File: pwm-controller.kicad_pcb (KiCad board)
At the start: 2 copper layers, 50 x 50 mm, 75 parts, among them J2 OUT-, J4 POWER, J5 OUT+, J6 DEBUG, J7 I2C, Q1 AO3400A, Q10 MMBT5551, Q11 MMBT5551, Q12 MMBT5401, Q2 AO3400A, Q3 AO3400A, Q4 AO3400A, Q5 AO3400A, Q6 AO3400A, Q7 MMBT5551, Q8 MMBT5551, Q9 MMBT5401, SW1 EC12D1524403, U1 L78L09_SOT89, U3 STM8S003F3Px, U4 HT7533-1-SOT89

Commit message: ready?
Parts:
- removed C13, C14, C15, C16, C17, C18, C19, C20: 100n/50, Capacitor_SMD:C_0402_1005Metric
- removed C9: 1u/50, Capacitor_SMD:C_0603_1608Metric
- removed Q11, Q8: MMBT5551, Package_TO_SOT_SMD:SOT-23
- removed Q3, Q6: AO3400A, Package_TO_SOT_SMD:SOT-23
- removed R18, R23, R25, R27: 4.7k, Resistor_SMD:R_0402_1005Metric
- removed R19, R28: 1k, Resistor_SMD:R_0402_1005Metric
- removed U4: HT7533-1-SOT89, Package_TO_SOT_SMD:SOT-89-3
- added TP1: TP5V, TestPoint:TestPoint_Pad_D2.0mm, F.Cu at (95.2, 87.3)
- C3, C4: value 100n/50 -> 3.3n
- Q1, Q2, Q4, Q5: value AO3400A -> NTMS4807; footprint Package_TO_SOT_SMD:SOT-23 -> mark:NTMS-4807N-SOIC-8-3.9x4.9x1.27P
- R1, R17, R3: value 4.7k -> 220
- R15, R16: value 120 -> 220
- R2, R24: value 120 -> 4.7k
- U1: value L78L09_SOT89 -> 78L05
- moved R1 20.4 mm to (104.8, 86.2)
- moved R3 13.6 mm to (104.8, 89.2)
- moved R20 13.2 mm to (107.4, 95.5), turned to 180 degrees
- moved C10 13.2 mm to (110.3, 94.7), turned to 180 degrees
- moved Q10 11.4 mm to (121.0, 97.2)
- moved Q12 11.4 mm to (114.7, 97.2)
- moved Q9 11.2 mm to (104.3, 97.2)
- moved Q7 11.2 mm to (110.6, 97.2)
- moved R12 11.2 mm to (97.2, 90.1), turned to 180 degrees
- moved C4 11.0 mm to (117.9, 98.5)
- moved R24 11.0 mm to (117.9, 97.2)
- moved C3 10.9 mm to (107.4, 98.5)
- moved R2 10.9 mm to (107.4, 97.2)
- moved R17 10.8 mm to (104.8, 87.7), turned to 180 degrees
- moved C2 10.2 mm to (94.6, 91.5), turned to 270 degrees
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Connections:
- C10 pad 1: +9V -> +5V
- C2 pad 1: +9V -> +5V
- C5 pad 1: +9V -> +5V
- C8 pad 2: +3V3 -> +5V
- Q10 pad 1: Net-(Q10-Pad1) -> PWM2
- Q10 pad 3: +9V -> +5V
- Q12 pad 1: Net-(Q10-Pad1) -> PWM2
- Q7 pad 1: Net-(Q7-Pad1) -> PWM1
- Q7 pad 3: +9V -> +5V
- Q9 pad 1: Net-(Q7-Pad1) -> PWM1
- R1 pad 1: +9V -> Net-(R1-Pad1)
- R1 pad 2: Net-(Q7-Pad1) -> RE_I
- R10 pad 2: +3V3 -> +5V
- R11 pad 2: +3V3 -> +5V
- R12 pad 2: +9V -> +5V
- R14 pad 2: +3V3 -> +5V
- R15 pad 2: +3V3 -> +5V
- R16 pad 2: +3V3 -> +5V
- R17 pad 1: GND -> Net-(R17-Pad1)
- R17 pad 2: +3V3 -> RE_Q
- R20 pad 1: Net-(Q8-Pad1) -> PWM1
- R29 pad 1: Net-(Q11-Pad1) -> PWM2
- R3 pad 1: Net-(Q7-Pad1) -> RE_B
- R3 pad 2: Net-(Q8-Pad3) -> Net-(R3-Pad2)
- R4 pad 2: +3V3 -> +5V
- R5 pad 2: +3V3 -> +5V
- R6 pad 2: +3V3 -> +5V
- R7 pad 2: +3V3 -> +5V
- R8 pad 2: +3V3 -> +5V
- R9 pad 2: +3V3 -> +5V
- SW1 pad A: RE_I -> Net-(R1-Pad1)
- SW1 pad B: RE_Q -> Net-(R17-Pad1)
- SW1 pad S1: RE_B -> Net-(R3-Pad2)
- U1 pad 1: +9V -> +5V
- U3 pad 9: +3V3 -> +5V
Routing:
- net GND: track 190.3 -> 290.9 mm, vias 133 -> 212
- net +5V: track 0.00 -> 91.7 mm, vias 0 -> 7
- net +9V: track 71.7 -> 0.00 mm, vias 5 -> 0
- net +3V3: track 60.0 -> 0.00 mm, vias 2 -> 0
- net VIN: track 77.6 -> 97.3 mm, vias 33 -> 50
- net RE_Q: track 46.0 -> 26.4 mm
- net Net-(R17-Pad1): track 0.00 -> 18.3 mm
- net PWM2: track 31.8 -> 49.3 mm, vias 2 -> 4
- net /channel1/GATE: track 28.6 -> 42.5 mm
- net DRAIN1: track 25.9 -> 36.8 mm, vias 21 -> 30
- net DRAIN2: track 25.9 -> 36.8 mm, vias 21 -> 30
- net /channel2/GATE: track 49.4 -> 60.3 mm, vias 2 -> 0
- net Net-(Q7-Pad1): track 10.7 -> 0.00 mm
- net Net-(Q10-Pad1): track 10.7 -> 0.00 mm
- net RE_B: track 33.3 -> 24.3 mm
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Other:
- board text removed: "10A should cause up to 100mV noise on GND. Slotting GND plane to reduce noise in digital section."

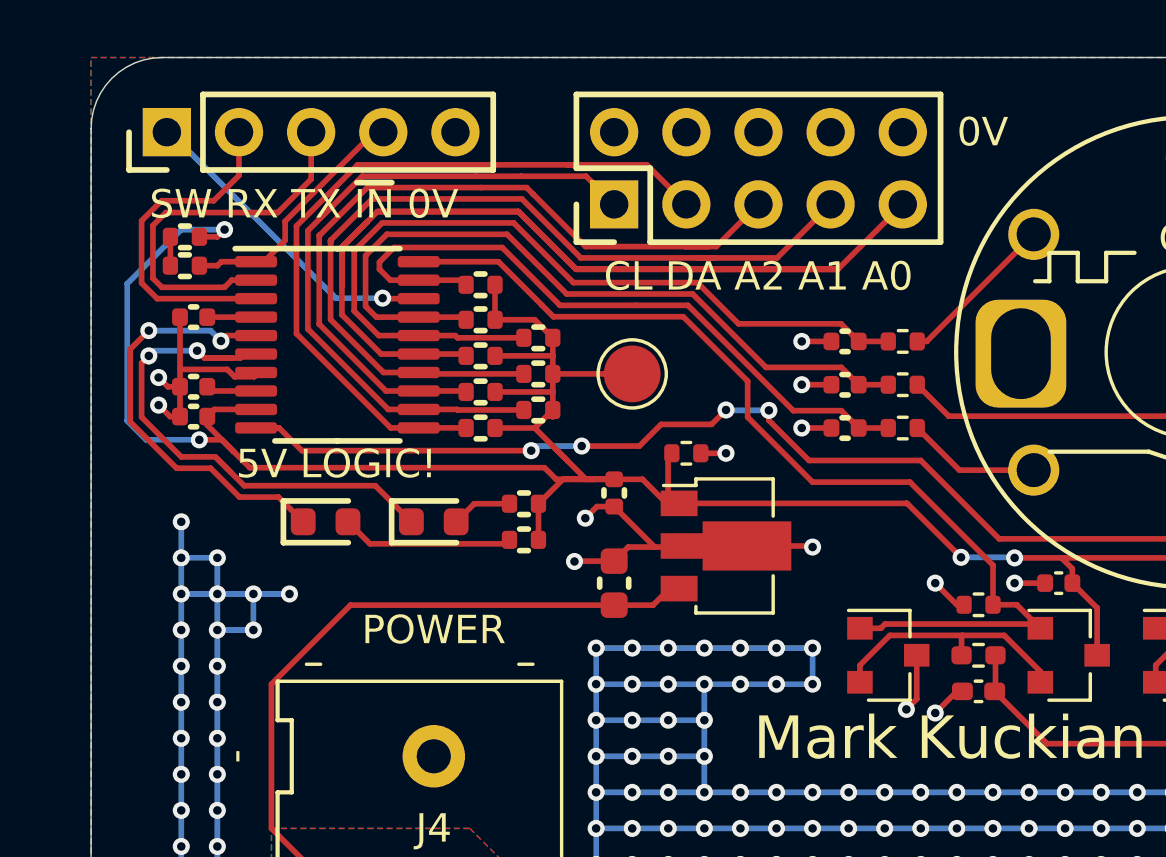
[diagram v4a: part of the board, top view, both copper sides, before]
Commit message: about to remove most pullups (use internals instead) and reroute IOs
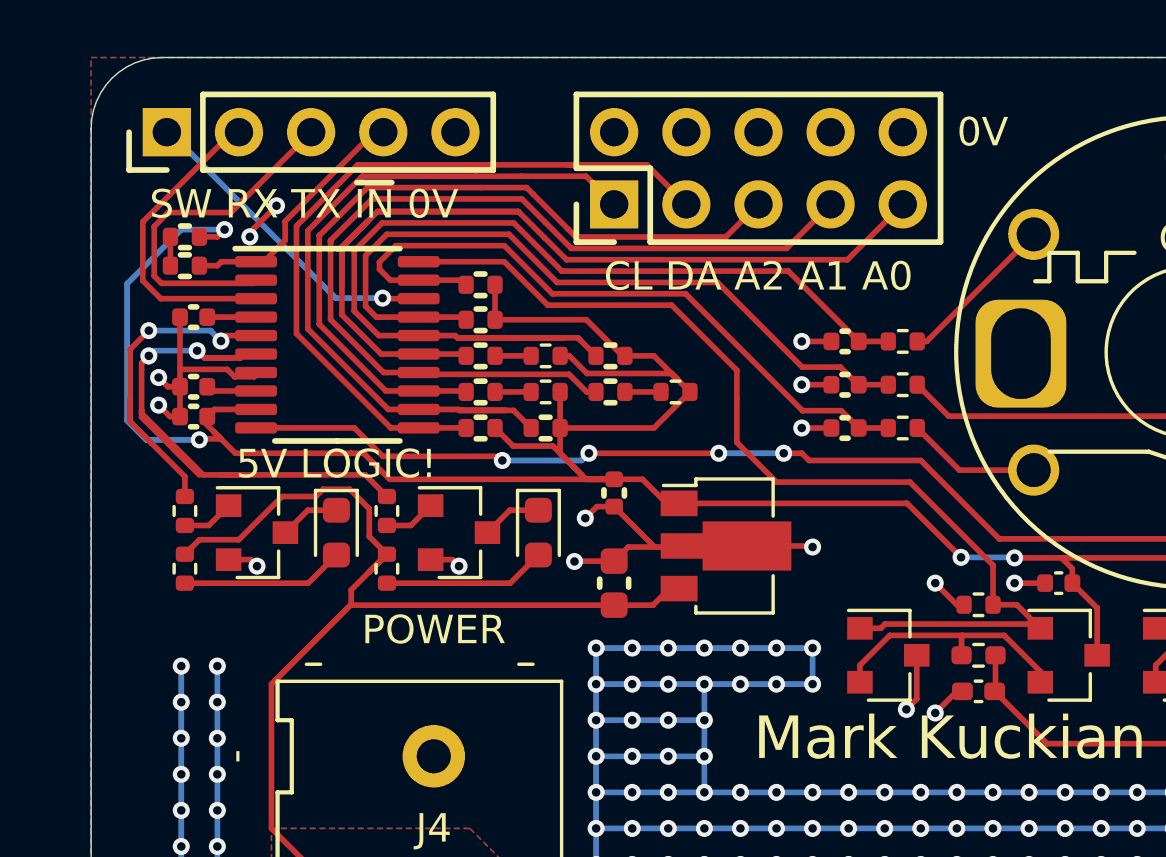
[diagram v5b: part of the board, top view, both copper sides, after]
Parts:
- removed TP1: TP5V, TestPoint:TestPoint_Pad_D2.0mm
- added Q3: MMBT5551, Package_TO_SOT_SMD:SOT-23, F.Cu at (82.0, 92.9)
- added Q6: MMBT5551, Package_TO_SOT_SMD:SOT-23, F.Cu at (89.2, 92.9)
- added R18: 220, Resistor_SMD:R_0402_1005Metric, F.Cu at (86.6, 94.2)
- added R19: 4.7k, Resistor_SMD:R_0402_1005Metric, F.Cu at (92.2, 88.0)
- added R21: 4.7k, Resistor_SMD:R_0402_1005Metric, F.Cu at (96.8, 88.0)
- added R22: 4.7k, Resistor_SMD:R_0402_1005Metric, F.Cu at (92.2, 86.7)
- R16: value 220 -> 4.7k
- moved R12 17.8 mm to (79.5, 92.2), turned to 90 degrees
- moved R15 12.0 mm to (79.5, 94.2), turned to 90 degrees
- moved R16 4.83 mm to (86.6, 92.2), turned to 90 degrees
- moved D2 3.70 mm to (91.9, 92.9), turned to 270 degrees
- moved R6 2.62 mm to (94.5, 86.7)
- moved R9 2.62 mm to (94.5, 88.0)
- moved R4 0.69 mm to (92.2, 89.2)
- moved D1 0.54 mm to (84.8, 92.9), turned to 270 degrees
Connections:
- net Net-(D1-Pad2) renamed /led_driver1/LED_A
- D1 pad 1: LED1 -> /led_driver1/LED_K
- D2 pad 1: LED2 -> /led_driver2/LED_K
- D2 pad 2: Net-(D2-Pad2) -> /led_driver2/LED_A
- R11 pad 2: +5V -> Net-(R11-Pad2)
- R12 pad 1: GND -> Net-(Q3-Pad1)
- R12 pad 2: +5V -> LED1
- R15 pad 2: +5V -> VIN
- R16 pad 1: Net-(D2-Pad2) -> Net-(Q6-Pad1)
- R16 pad 2: +5V -> LED2
- R7 pad 2: +5V -> Net-(R19-Pad1)
- R9 pad 2: +5V -> Net-(R21-Pad1)
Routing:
- net SADD0: track 55.6 -> 36.7 mm
- net VIN: track 97.3 -> 113.7 mm
- net GND: track 290.9 -> 277.2 mm, vias 212 -> 205
- net RE_I: track 29.4 -> 35.9 mm
- net /led_driver2/LED_A: track 0.00 -> 5.75 mm
- net +5V: track 91.7 -> 94.1 mm
- net LED2: track 19.1 -> 21.4 mm
- net LED1: track 15.0 -> 12.8 mm
- net SCL: track 24.3 -> 26.4 mm
- net Net-(D2-Pad2): track 2.14 -> 0.00 mm
- net /led_driver1/LED_K: track 0.00 -> 2.12 mm
- net /led_driver2/LED_K: track 0.00 -> 2.12 mm
- net SADD1: track 30.9 -> 32.8 mm
- net Net-(Q3-Pad1): track 0.00 -> 1.83 mm
- net Net-(Q6-Pad1): track 0.00 -> 1.83 mm
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
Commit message: ready to order?
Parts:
- removed the C2 at (94.6, 91.5)
- removed the H4 at (123.0, 79.4)
- removed the H4 at (123.0, 123.0)
- removed the J6 at (78.9, 78.8)
- removed J7: I2C, Connector_PinHeader_2.54mm:PinHeader_2x05_P2.54mm_Vertical
- removed the R10 at (89.9, 84.2)
- removed the R11 at (89.9, 86.7)
- removed the R13 at (79.5, 83.5)
- removed the R14 at (79.5, 82.5)
- removed R19, R21, R22: 4.7k, Resistor_SMD:R_0402_1005Metric
- removed the R5 at (89.9, 89.2)
- removed the R6 at (94.5, 86.7)
- removed the R7 at (89.9, 88.0)
- removed the R8 at (89.9, 85.4)
- removed the R9 at (94.5, 88.0)
- added C3: 3.3n, Capacitor_SMD:C_0402_1005Metric, F.Cu at (90.9, 87.1)
- added C5: 100n/50, Capacitor_SMD:C_0402_1005Metric, F.Cu at (95.8, 92.2)
- added D1: B5819W SL, Diode_SMD:D_SOD-123, F.Cu at (93.5, 99.1)
- added H3: M2, MountingHole:MountingHole_2mm, F.Cu at (93.5, 110.0)
- added H5: M2, MountingHole:MountingHole_2.2mm_M2, F.Cu at (123.0, 123.0)
- added H6: M2, MountingHole:MountingHole_2mm, F.Cu at (123.5, 110.0)
- added H8: M2, MountingHole:MountingHole_2.2mm_M2, F.Cu at (123.0, 79.4)
- added J1: DEBUG_ADDRESS_I2C_INT, Connector_PinHeader_2.54mm:PinHeader_2x09_P2.54mm_Horizontal, F.Cu at (79.5, 82.8)
- added R1: 220, Resistor_SMD:R_0402_1005Metric, F.Cu at (90.7, 90.9)
- added R2: 220, Resistor_SMD:R_0402_1005Metric, F.Cu at (90.7, 91.9)
- added R3: 4.7k, Resistor_SMD:R_0402_1005Metric, F.Cu at (97.3, 87.9)
- moved R4 7.24 mm to (99.3, 87.9), turned to 180 degrees
- moved J4 4.07 mm to (85.1, 105.9)
- moved R13 2.59 mm to (80.0, 96.7)
- moved U1 2.59 mm to (85.4, 88.9)
- moved R15 2.59 mm to (87.1, 96.7)
- moved D3 2.59 mm to (92.5, 95.5)
- moved Q10 2.59 mm to (89.7, 95.5)
- moved R12 2.59 mm to (80.0, 94.7)
- moved C1 2.59 mm to (80.3, 90.3)
- moved C2 2.59 mm to (80.3, 91.4)
- moved C6 2.59 mm to (80.3, 87.9)
- moved D2 2.59 mm to (85.3, 95.5)
- moved Q9 2.59 mm to (82.5, 95.5)
- moved R14 2.59 mm to (87.1, 94.7)
- moved C9 1.92 mm to (103.0, 87.3)
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- renumbered C6 to C1, C5 to C10, C3 to C11, C10 to C12, C4 to C13, C8 to C2, C1 to C4, C7 to C6, C21 to C7, C22 to C8, C23 to C9, D1 to D2, D2 to D3, H5 to H4, J2 to J6, Q7 to Q1, Q6 to Q10, Q9 to Q2, Q1 to Q3, Q2 to Q4, Q10 to Q5, Q12 to Q6, Q4 to Q7, Q5 to Q8, Q3 to Q9, R24 to R10, R29 to R11, R15 to R13, R16 to R14, R18 to R15, R1 to R5, R3 to R6, R17 to R7, R2 to R8, R20 to R9, U3 to U1, U1 to U2
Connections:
- C4 pad 1: VIN -> VIN_D
- R13 pad 2: VIN -> VIN_D
- R15 pad 2: VIN -> VIN_D
- R4 pad 1: SCL -> SDA
- U1 pad 10: PWM2 -> PWM1
- U1 pad 11: SDA -> /SDA_PIN
- U1 pad 12: SCL -> /SCL_PIN
- U1 pad 13: SADD2 -> RE_B
- U1 pad 14: SADD1 -> RE_Q
- U1 pad 15: SADD0 -> RE_I
- U1 pad 16: RE_I -> SADD2
- U1 pad 17: RE_Q -> SADD1
- U1 pad 19: RE_B -> SADD0
- U1 pad 20: PWM1 -> PWM2
- U2 pad 3: VIN -> VIN_D
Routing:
- net +5V: track 94.1 -> 59.1 mm
- net SADD0: track 36.7 -> 8.32 mm
- net VIN_D: track 0.00 -> 28.1 mm
- net SADD1: track 32.8 -> 7.11 mm
- net VIN: track 113.7 -> 93.1 mm, vias 50 -> 47
- net SADD2: track 26.6 -> 7.04 mm
- net RE_I: track 35.9 -> 18.4 mm, vias 0 -> 2
- net GND: track 277.2 -> 289.5 mm, vias 205 -> 201
- net SCL: track 26.4 -> 16.6 mm
- net INT: track 8.98 -> 18.6 mm, vias 0 -> 2
- net RE_Q: track 26.4 -> 18.5 mm, vias 0 -> 2
- net SDA: track 26.9 -> 19.1 mm
- net DRAIN2: track 36.8 -> 44.4 mm, vias 30 -> 32
- net DRAIN1: track 36.8 -> 44.5 mm, vias 30 -> 32
- net UTX: track 12.4 -> 4.82 mm
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- added copper zone on In1.Cu, net GND
- added copper zone on In2.Cu, net GND
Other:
- copper layers 2 -> 4
- board text added: "Basically a (JLC-compatible) 2-layer board design, but done as 4-layer (with ground-fills for inner layers) for better thermals."
- board text removed: "0V"
- board text removed: "CL DA A2 A1 A0"
- board text removed: "SW RX TX ~IN~ 0V"

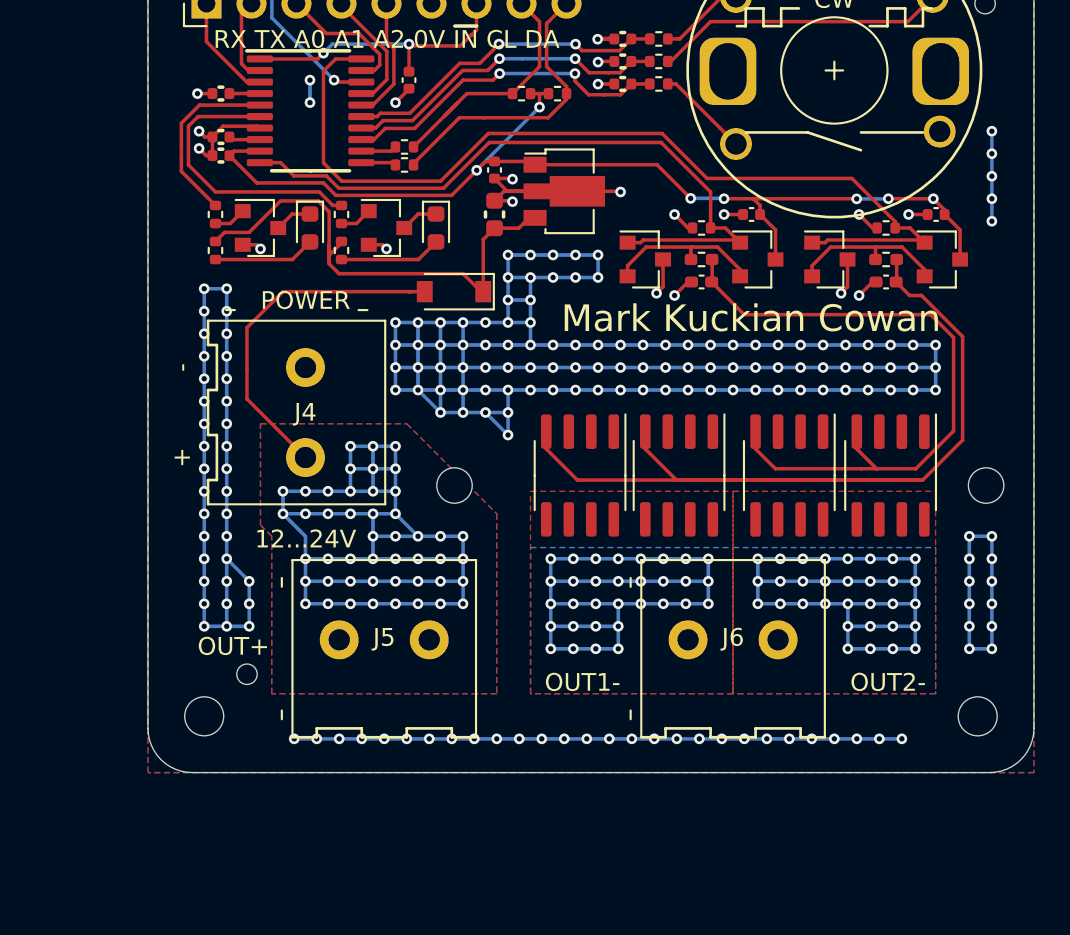
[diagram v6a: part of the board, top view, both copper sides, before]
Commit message: moved screw terminals to edge of board, reduced stitching/thermal-via frequency
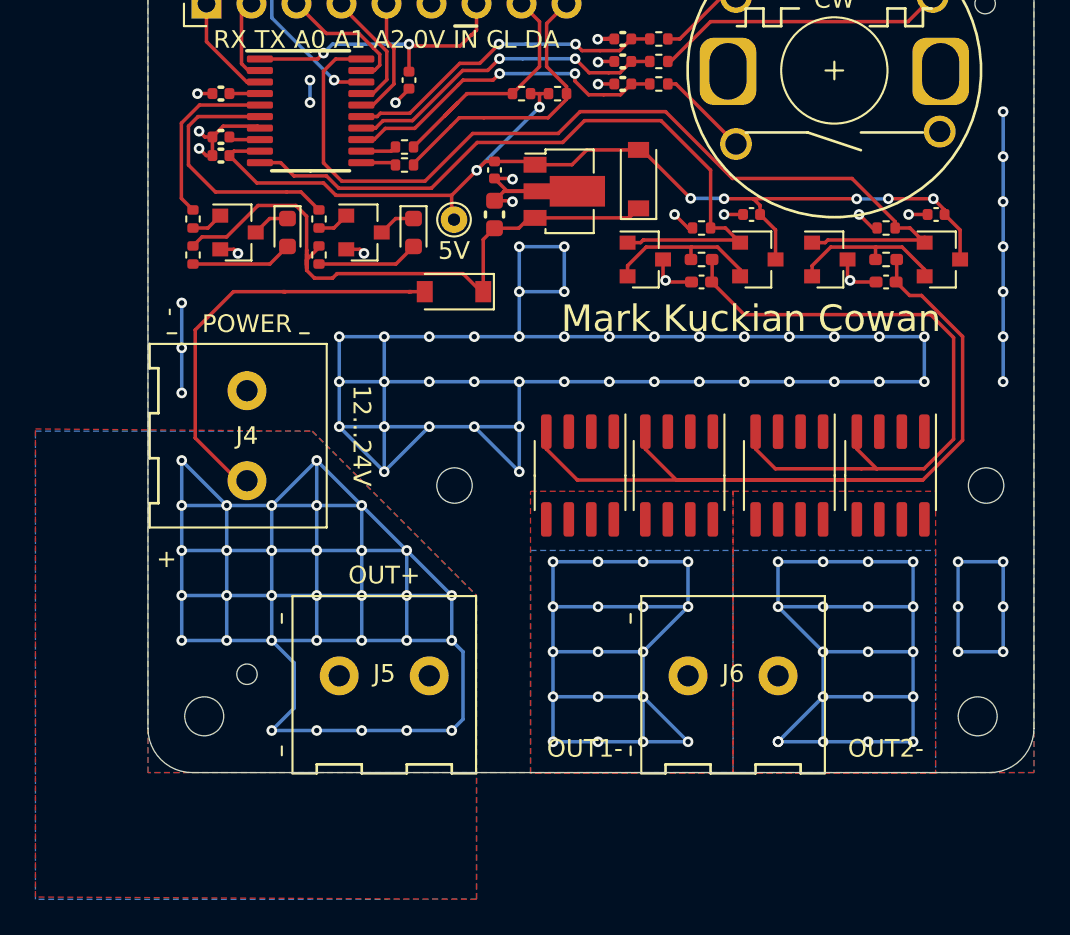
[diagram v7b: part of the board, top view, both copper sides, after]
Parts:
- added D4: B5819W SL, Diode_SMD:D_SOD-123, F.Cu at (103.9, 92.7)
- added TP1: 5V, TestPoint:TestPoint_THTPad_D1.5mm_Drill0.7mm, F.Cu at (93.5, 95.0)
- moved J4 3.55 mm to (81.8, 107.2)
- moved J5 2.03 mm to (89.5, 120.7)
- moved J6 2.03 mm to (109.2, 120.7)
- moved Q10 1.30 mm to (88.4, 95.7)
- moved R12 1.30 mm to (78.7, 95.0)
- moved R13 1.30 mm to (78.7, 97.0)
- moved D2 1.30 mm to (84.1, 95.7)
- moved D3 1.30 mm to (91.2, 95.7)
- moved Q9 1.30 mm to (81.3, 95.7)
- moved R14 1.30 mm to (85.9, 95.0)
- moved R15 1.30 mm to (85.9, 97.0)
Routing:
- net GND: track 289.5 -> 188.5 mm, vias 201 -> 74
- net VIN: track 93.1 -> 168.1 mm, vias 47 -> 32
- net DRAIN2: track 44.4 -> 58.0 mm, vias 32 -> 18
- net DRAIN1: track 44.5 -> 58.0 mm, vias 32 -> 19
- net VIN_D: track 28.1 -> 36.8 mm
- net +5V: track 59.1 -> 61.2 mm
- net PWM1: track 38.8 -> 40.5 mm
- net LED2: track 16.0 -> 14.9 mm
- net PWM2: track 52.9 -> 54.0 mm
